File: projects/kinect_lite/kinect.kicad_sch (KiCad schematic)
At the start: 22 parts, among them J2 USB_C_Receptacle_USB2.0_16P, J3 Conn_02x05_Odd_Even, U1 LM3670MFX-1.8, U2 AP63203WU

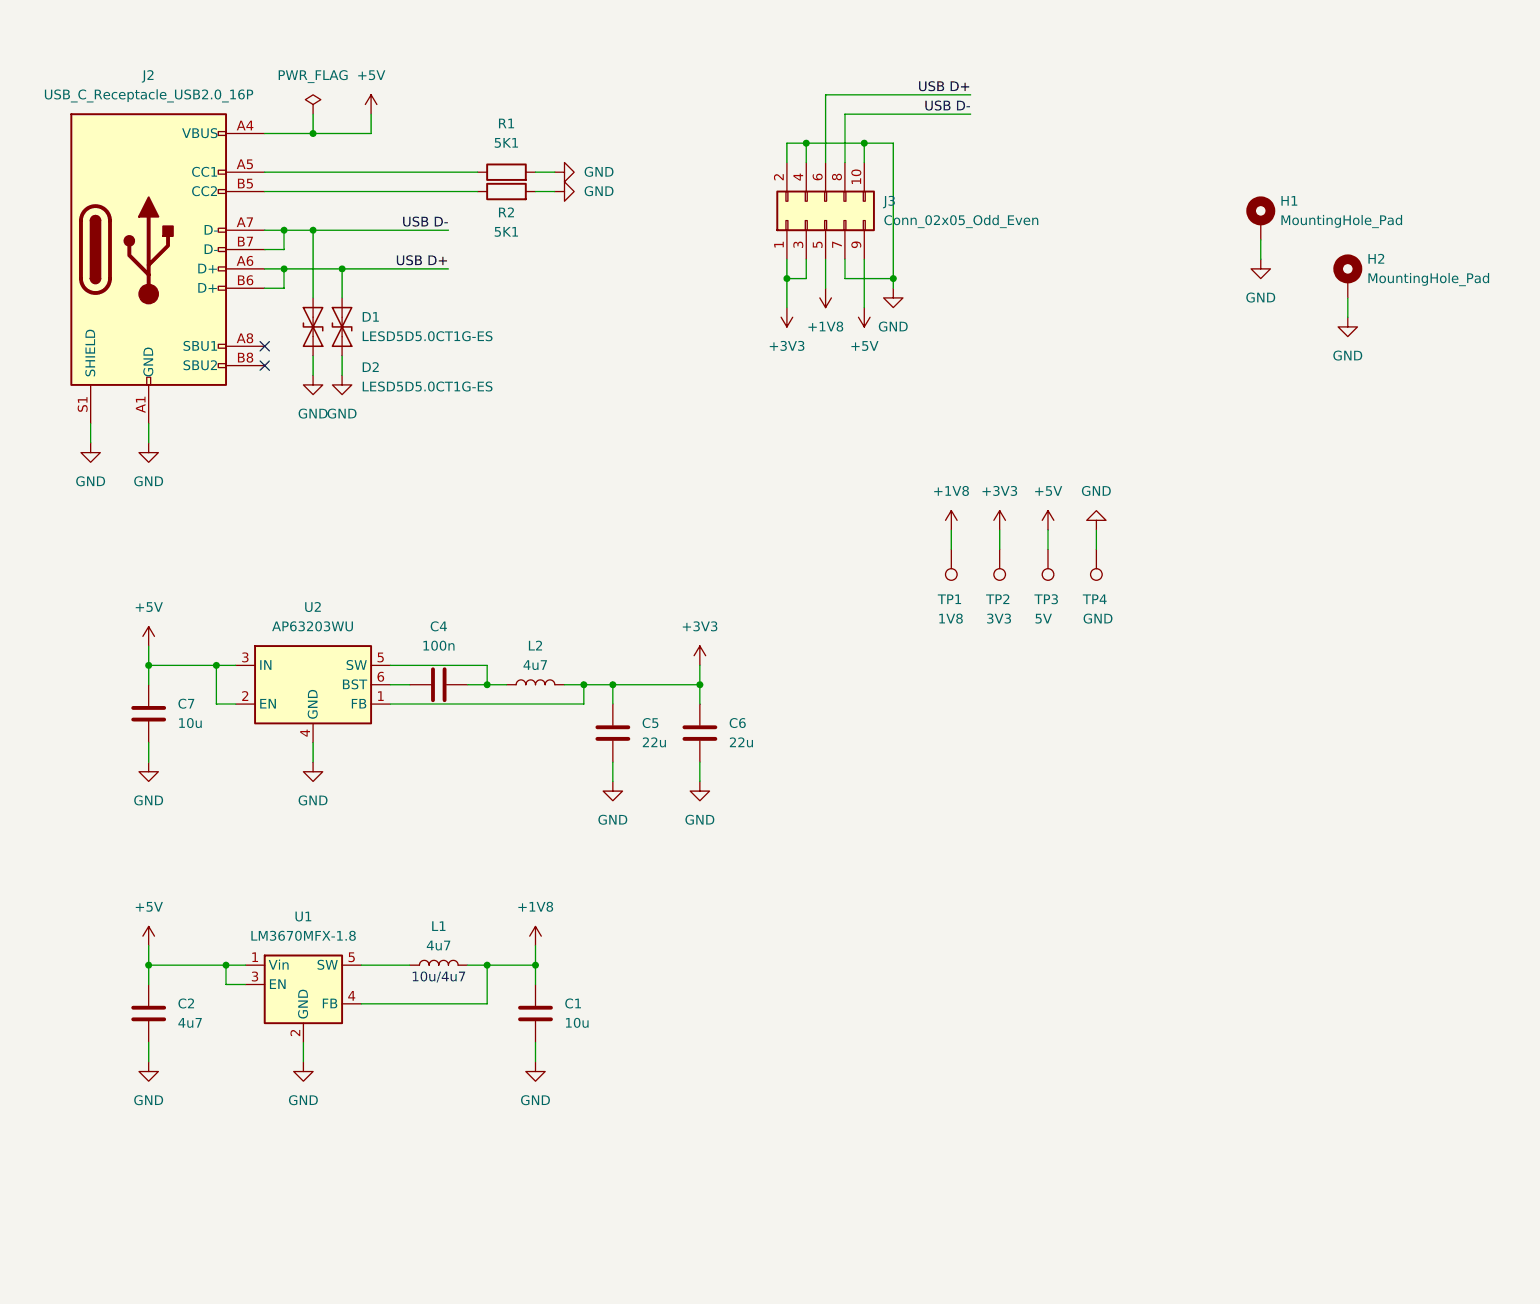
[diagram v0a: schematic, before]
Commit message: Finish v1 of kinect_lite
Modify silkscreen
Add graphics to copper layer (designed wuth kicad and duckie robot)
round corners of outline
generate Gerbers

Create v2 and v3 of 3D printed cover in FreeCAD
export STL for 3D printing
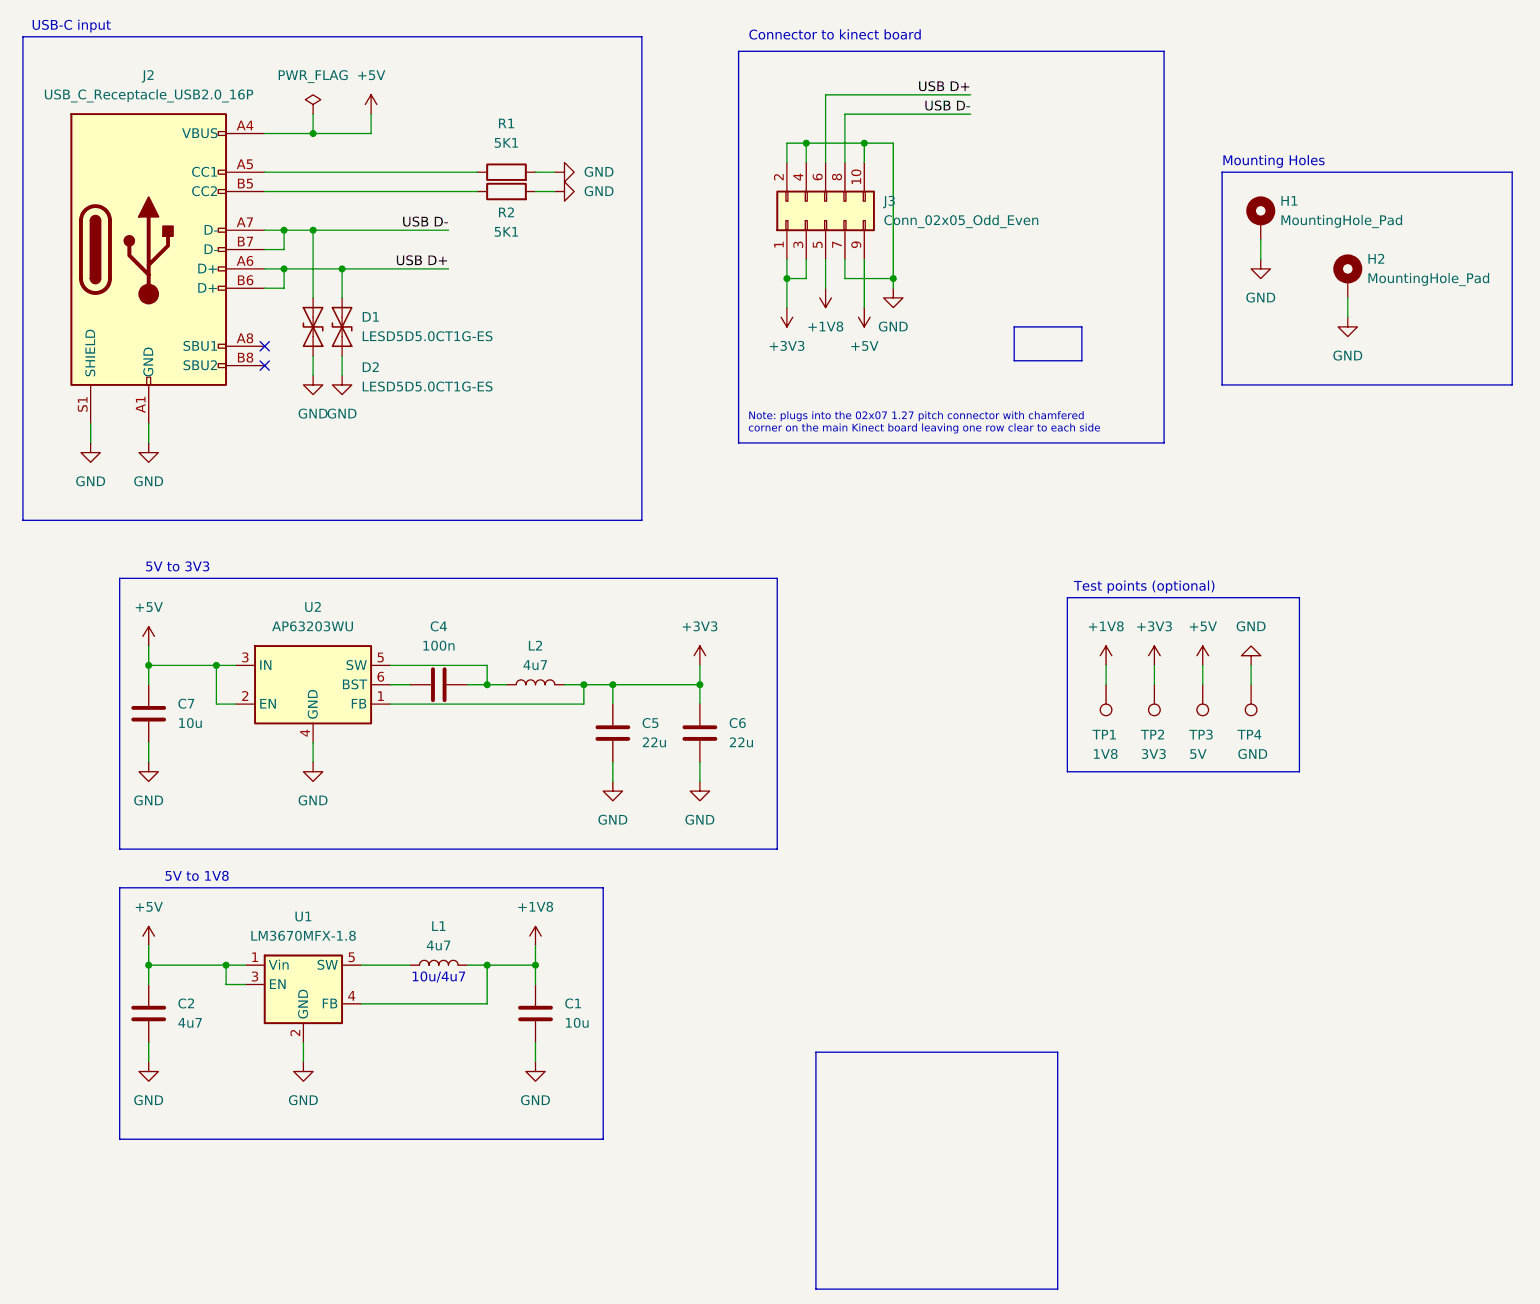
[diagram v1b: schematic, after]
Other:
- note added: "5V to 1V8"
- note added: "5V to 3V3"
- note added: "Connector to kinect board"
- note added: "Mounting Holes"
- note added: "Note: plugs into the 02x07 1.27 pitch connector with chamfered corner on the main Kinect board leaving one row clear to each side"
- note added: "Test points (optional)"
- note added: "USB-C input"
- company: (none) -> sevillabot
- title: (none) -> Kinect Lite Board
- moved on the sheet: TP1, TP2, TP3, TP4
